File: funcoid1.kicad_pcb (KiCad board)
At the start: 2 copper layers, 100 x 100 mm, 40 parts, among them J1 7-15V DC, J2 NMI_CTRL, J3 IRQ_CTRL, J4 BREAKOUT, J5 S1_SERIAL, SW1 SW_RST, U1 74HC132, U2 HM62256ALP-10, U3 WD65C02, U4 W65C51N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

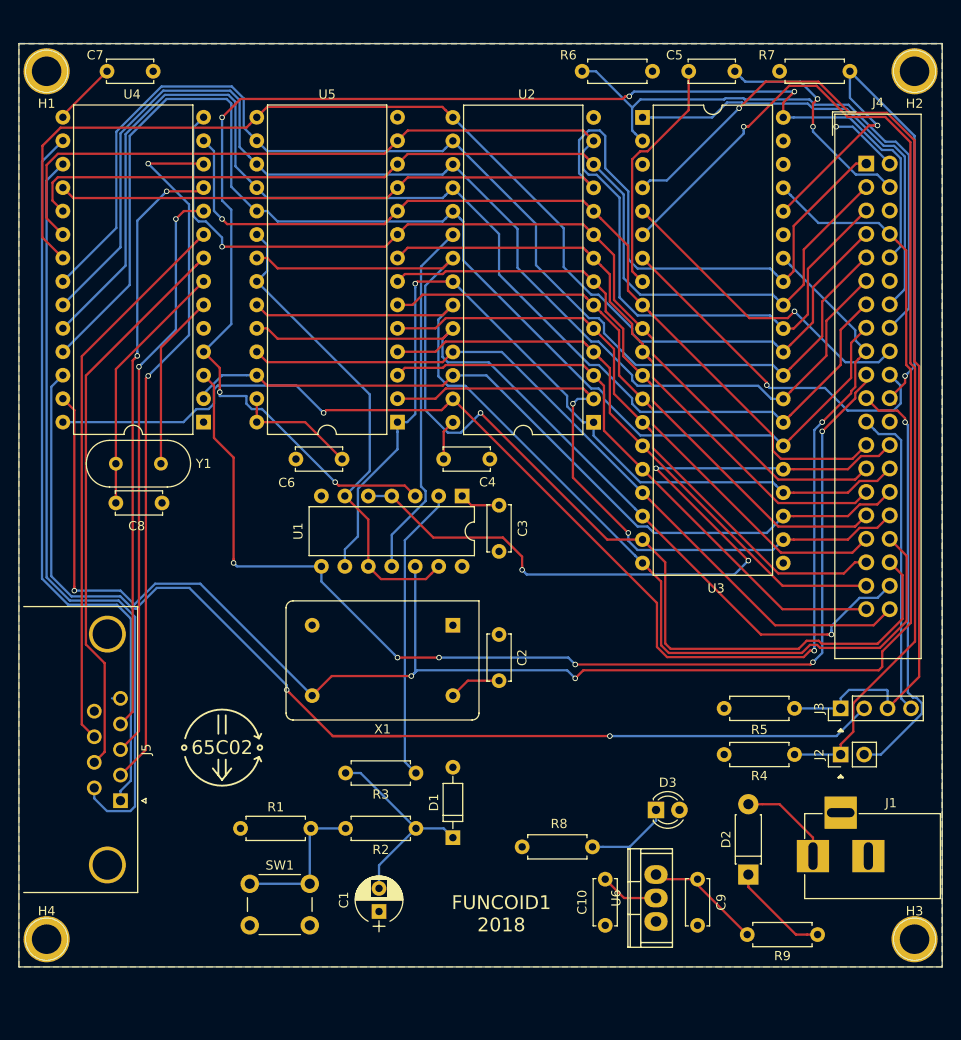
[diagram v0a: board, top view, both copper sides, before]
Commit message: Use a ZIF footprint for U5 (EEPROM)
ZIF sockets have feet that are slightly too wide to fit in a regular DIP
footprint's drill holes. This caused me issues in the fist spin of
FUNCOID1. Replace it with a ZIF footprint as was originally envisaged.

I had to upgrade to KiCad 5 to make use of these new footprints. I made
a custom derivative where the ZIF lever is facing the other way, but
preserving the orientation of the pads.

Some components had to be shifted around a little to avoid overlapping
courtyards.
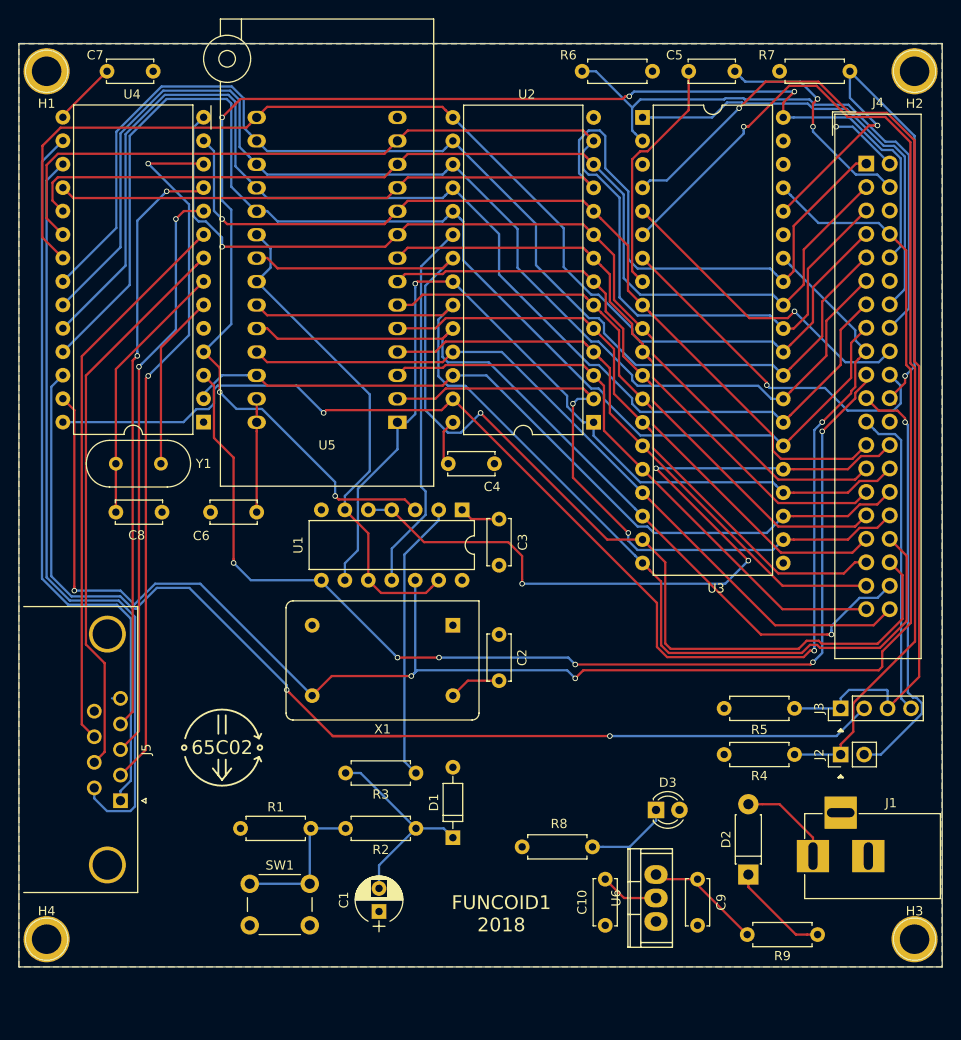
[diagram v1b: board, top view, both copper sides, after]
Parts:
- U5: footprint Housings_DIP:DIP-28_W15.24mm -> custom:DIP_Socket-28_W11.9_W12.7_W15.24_W17.78_W18.5_3M_228-1277-00-0602J_rotated
- moved U5 36.4 mm to (125.8, 57.0), turned to 0 degrees
- moved C6 10.9 mm to (125.8, 99.8)
- moved C3 1.50 mm to (152.0, 100.5)
- moved U1 1.50 mm to (148.0, 99.5)
- moved C8 1.00 mm to (110.5, 99.8)
- moved C4 0.71 mm to (146.5, 94.5)
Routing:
- net ROM_SEL: track 52.9 -> 54.7 mm
- net /A14: track 97.9 -> 99.5 mm
- net CLK: track 192.2 -> 190.7 mm
- net RAM_SEL: track 39.1 -> 40.5 mm
- net Net-(R3-Pad1): track 32.0 -> 30.6 mm
- net VCC: track 75.2 -> 74.0 mm
- net /A15: track 86.7 -> 87.8 mm
- net IO_SEL: track 123.6 -> 122.6 mm
- net Net-(C8-Pad1): track 27.9 -> 28.9 mm
- net RESET: track 150.9 -> 151.7 mm

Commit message: Add a MAX232 for proper RS-232 signalling
Use a MAX232 to drive the signal on the DB9 connector, such that it is
RS-232 compliant and will be understood by my VT510 terminal. Route the
old 5V CMOS UART to a new 6-pin header for use with an FTDI.

This change also moves the DB9 connector to the same edge as the barrel
jack, which should make designing a box a little easier.

Finally, do some general re-routing on the PCB layout.
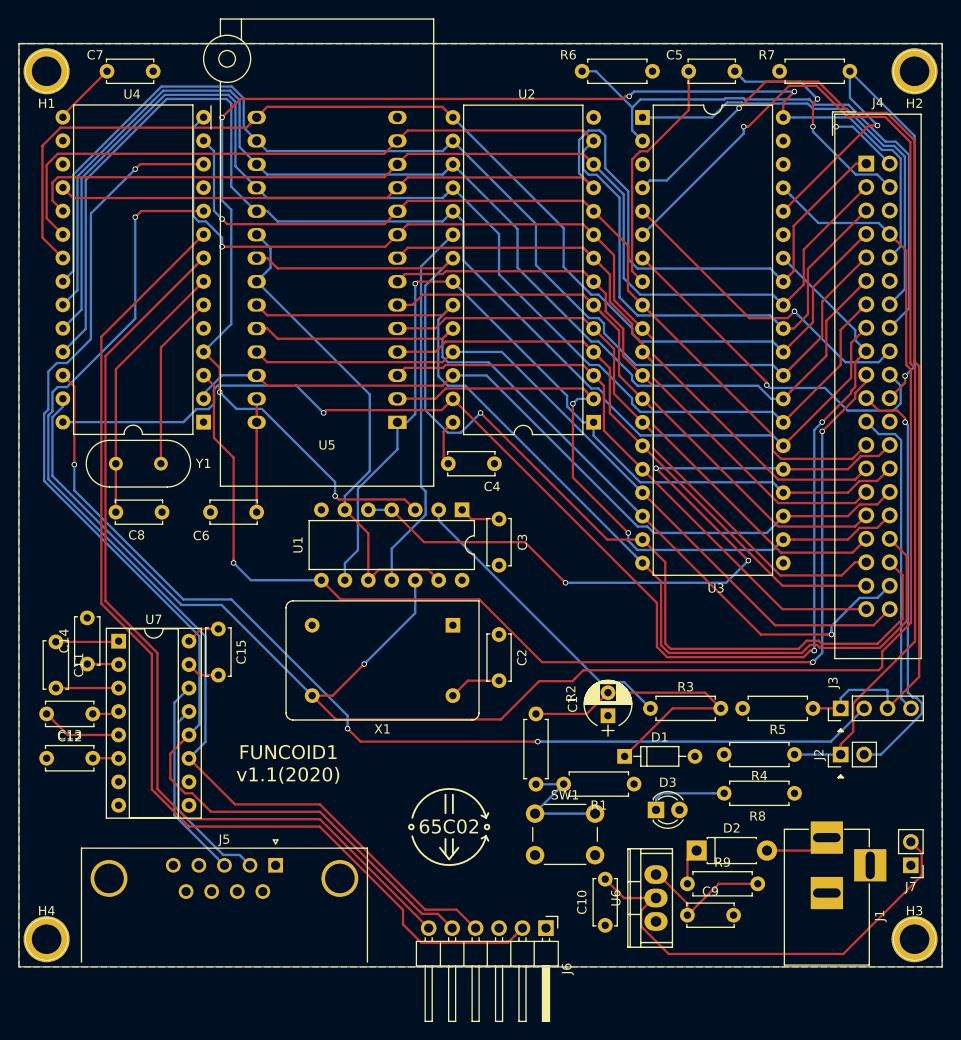
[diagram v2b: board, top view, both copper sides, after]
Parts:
- added C11: 1u, Capacitor_THT:C_Disc_D5.0mm_W2.5mm_P5.00mm, F.Cu at (104.0, 113.8)
- added C12: 1u, Capacitor_THT:C_Disc_D5.0mm_W2.5mm_P5.00mm, F.Cu at (108.0, 121.6)
- added C13: 1u, Capacitor_THT:C_Disc_D5.0mm_W2.5mm_P5.00mm, F.Cu at (103.0, 126.4)
- added C14: 1u, Capacitor_THT:C_Disc_D5.0mm_W2.5mm_P5.00mm, F.Cu at (107.4, 116.2)
- added C15: 1u, Capacitor_THT:C_Disc_D5.0mm_W2.5mm_P5.00mm, F.Cu at (121.6, 112.4)
- added J6: S1_CMOS, Connector_PinHeader_2.54mm:PinHeader_1x06_P2.54mm_Horizontal, F.Cu at (157.1, 144.8)
- added J7: 5V DC, Connector_PinHeader_2.54mm:PinHeader_1x02_P2.54mm_Vertical, F.Cu at (196.6, 138.0)
- added U7: MAX232_Small, Package_DIP:DIP-16_W7.62mm_Socket, F.Cu at (110.8, 113.7)
- J5: value S1_SERIAL -> S1_RS232
- moved R1 42.9 mm to (166.6, 129.2), turned to 180 degrees
- moved C1 32.6 mm to (163.8, 121.8)
- moved SW1 31.8 mm to (155.9, 132.4)
- moved R8 30.1 mm to (184.0, 130.2), turned to 180 degrees
- moved R3 26.3 mm to (168.4, 121.0), turned to 0 degrees
- moved D1 20.6 mm to (165.6, 126.2), turned to 0 degrees
- moved J5 18.2 mm to (127.8, 138.0), turned to 0 degrees
- moved R2 18.0 mm to (156.0, 121.6), turned to 270 degrees
- moved R9 15.1 mm to (172.4, 140.0), turned to 0 degrees
- moved D2 6.17 mm to (173.4, 136.4), turned to 0 degrees
- moved C9 4.05 mm to (172.4, 143.4), turned to 0 degrees
- moved J1 2.50 mm to (187.5, 135.0), turned to 90 degrees
- moved R5 2.00 mm to (186.0, 121.0)
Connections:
- J5 pad 1: /S1_DCD -> Net-(J5-Pad1)
- J5 pad 2: /S1_RX -> Net-(J5-Pad2)
- J5 pad 3: /S1_TX -> Net-(J5-Pad3)
- J5 pad 4: /S1_DTR -> Net-(J5-Pad4)
- J5 pad 6: /S1_DSR -> Net-(J5-Pad6)
- J5 pad 7: /S1_RTS -> Net-(J5-Pad7)
- J5 pad 8: /S1_CTS -> Net-(J5-Pad8)
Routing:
- net /S1_DSR: track 83.7 -> 0.00 mm
- net /S1_DCD: track 80.0 -> 0.00 mm
- net /S1_DTR: track 63.9 -> 0.00 mm, vias 2 -> 0
- net /S1_CTS: track 60.4 -> 115.6 mm
- net /S1_TX: track 63.3 -> 117.2 mm, vias 2 -> 1
- net VCC: track 74.0 -> 120.9 mm
- net /S1_RX: track 77.2 -> 123.9 mm, vias 2 -> 1
- net /S1_RTS: track 61.2 -> 99.9 mm
- net Net-(J5-Pad3): track 0.00 -> 22.1 mm
- net Net-(J5-Pad2): track 0.00 -> 21.4 mm
- net S1_IRQ: track 128.3 -> 112.1 mm, vias 2 -> 3
- net Net-(C1-Pad2): track 22.7 -> 34.3 mm
- net Net-(C12-Pad2): track 0.00 -> 8.74 mm
- net Net-(D2-Pad1): track 11.0 -> 4.01 mm
- net Net-(C11-Pad1): track 0.00 -> 6.83 mm
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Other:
- board text added: "FUNCOID1 v1.1(2020)"
- board text removed: "FUNCOID1 2018"
